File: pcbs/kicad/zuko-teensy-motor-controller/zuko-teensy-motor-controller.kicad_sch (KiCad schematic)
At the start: 58 parts, among them J1 Conn_01x03, J10 Conn_01x03, J11 Conn_01x03, J12 Conn_01x03, J13 Conn_01x03, J14 Conn_01x02, J15 Conn_01x02, J16 Conn_01x02, J17 Conn_01x03, J18 Conn_01x03, J19 Conn_01x02, J2 Conn_01x03, J20 Conn_01x02, J21 Conn_01x02, J22 Conn_01x03, J24 Conn_01x04, J25 Conn_01x03, J26 Conn_01x03, J27 Conn_01x04, J28 Conn_01x04, J29 Conn_01x04, J3 Conn_01x03, J30 Conn_01x04, J31 Conn_01x04, J32 Conn_01x04, J33 Conn_01x04, J4 Conn_01x02, J5 Conn_01x03, J6 Conn_01x03, J7 Conn_01x03, J8 Conn_01x03, J9 Conn_01x03, Q1 BSS138, Q2 BSS138, U1 ACS712xLCTR-20A, U2 Teensy4.0, U3 ULN2003

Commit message: pcb update
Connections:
- net AUX_M1: now also J17.1 (Pin_1); no longer J17.2 (Pin_2)
- net AUX_M2: now also J18.1 (Pin_1); no longer J18.2 (Pin_2)
- net AUX_M3: now also J22.1 (Pin_1); no longer J22.2 (Pin_2)
- new net: J17.2 (Pin_2), J18.2 (Pin_2), J22.2 (Pin_2), JP1.2 (C)

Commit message: pcb update
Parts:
- added J23: Conn_01x02, Connector_PinHeader_2.54mm:PinHeader_1x02_P2.54mm_Vertical, symbol Connector_Generic:Conn_01x02
- J4: footprint Connector_AMASS:AMASS_XT60-F_1x02_P7.20mm_Vertical -> Connector_AMASS:AMASS_XT60-M_1x02_P7.20mm_Vertical
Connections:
- net +BATT: now also J23.1 (Pin_1)
- net GND: now also J23.2 (Pin_2)
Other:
- moved on the sheet: J21

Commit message: pcb update
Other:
- note added: "Aux. Servo Motor Interfaces"
- note added: "Contact Switches and LEDs"
- note added: "I2C Interfaces"
- note added: "Microcontroller"
- note added: "Neopixel LED Strip Interfaces"
- note added: "Power In, Current Sense, and Voltage Sense"
- note added: "Servo Motor Interfaces"
- note added: "UART Interface"
- moved on the sheet: C1, C2, C3, C4, C5, C6, J1, J10, J11, J12, J13, J14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

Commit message: pcb update
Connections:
- net GND: no longer U2.47 (GND)
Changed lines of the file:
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@@
   (junction (at 105.41 181.61) (diameter 0) (color 0 0 0 0)
   )
-  (junction (at 265.43 149.86) (diameter 0) (color 0 0 0 0)
-  )
   (junction (at 83.82 114.3) (diameter 0) (color 0 0 0 0)
   )
@@
     (stroke (width 0) (type default) (color 0 0 0 0))
   )
-  (wire (pts (xy 265.43 106.68) (xy 265.43 149.86))
-    (stroke (width 0) (type default) (color 0 0 0 0))
-  )
   (wire (pts (xy 363.22 222.25) (xy 363.22 223.52))
     (stroke (width 0) (type default) (color 0 0 0 0))
@@
     (stroke (width 0) (type default) (color 0 0 0 0))
   )
-  (wire (pts (xy 247.65 106.68) (xy 265.43 106.68))
-    (stroke (width 0) (type default) (color 0 0 0 0))
-  )

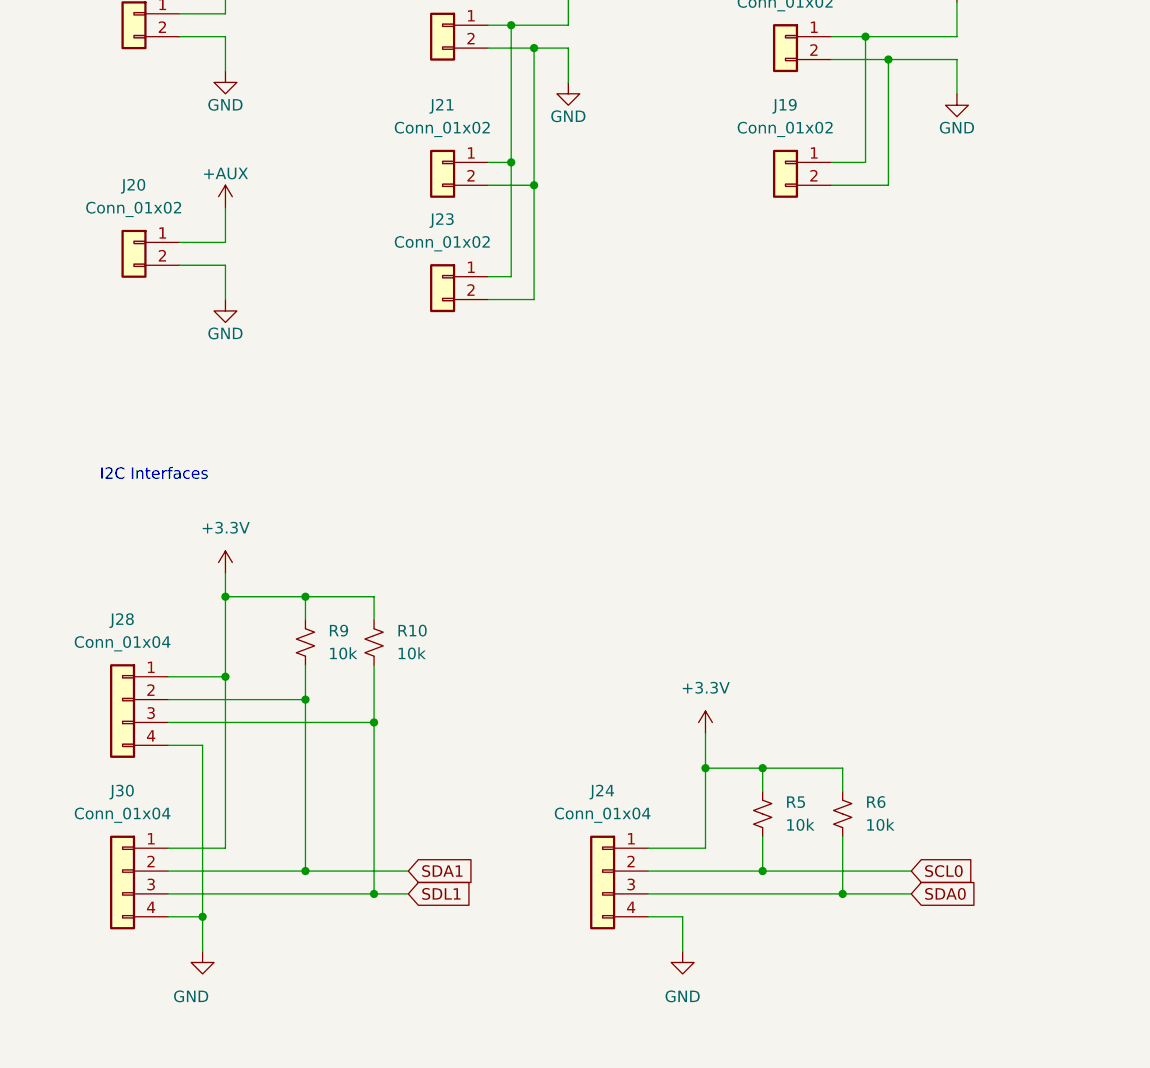
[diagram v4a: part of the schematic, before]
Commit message: pcb update - 2 layers to 4 layers
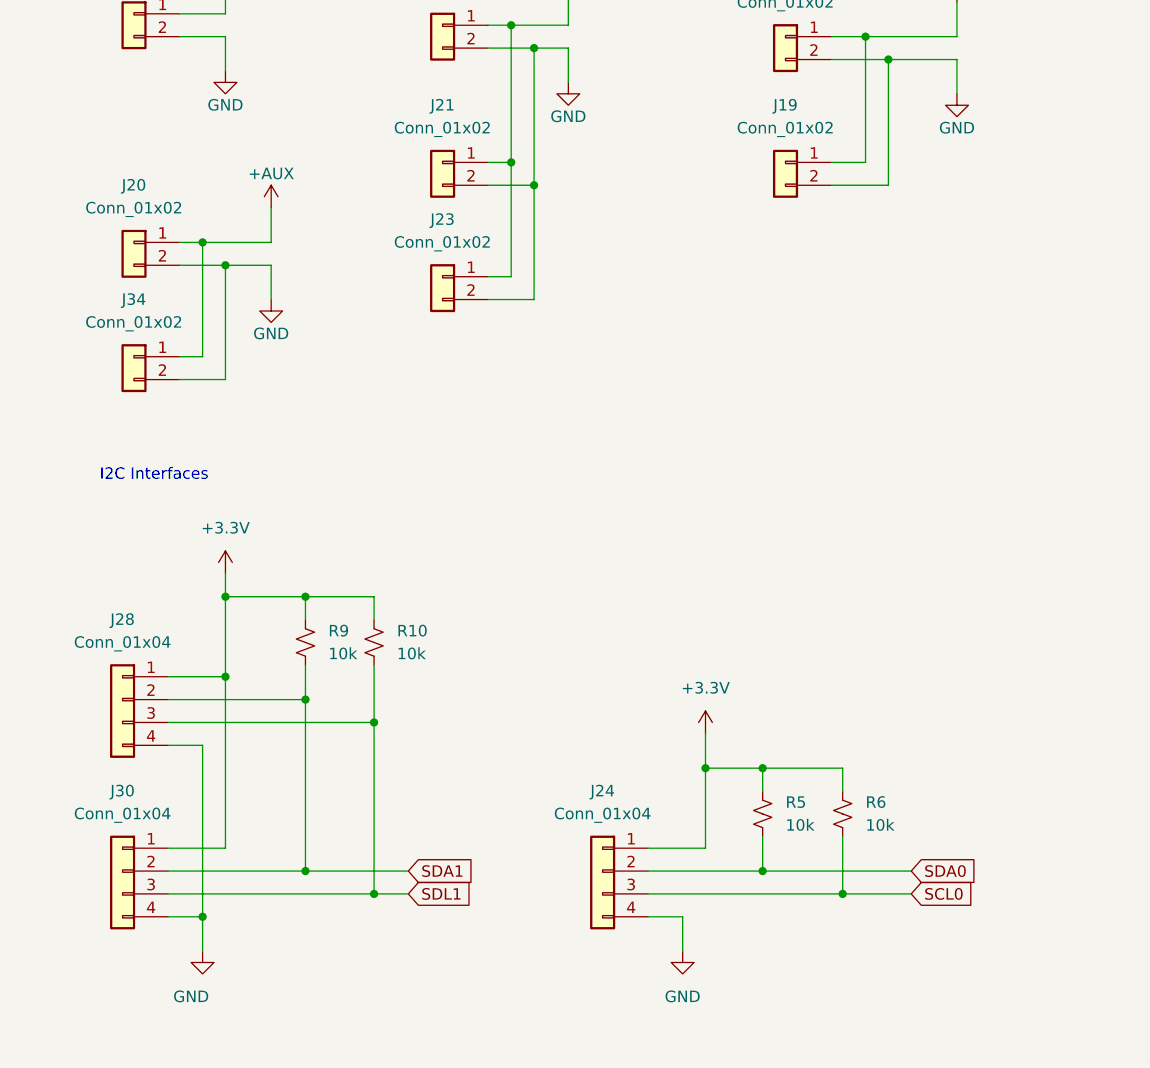
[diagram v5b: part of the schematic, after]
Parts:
- added J34: Conn_01x02, Connector_PinHeader_2.54mm:PinHeader_1x02_P2.54mm_Vertical, symbol Connector_Generic:Conn_01x02
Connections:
- net +AUX: now also J34.1 (Pin_1)
- net GND: now also J34.2 (Pin_2)
- net SCL0: now also J24.3 (Pin_3), R6.2; no longer J24.2 (Pin_2), R5.2
- net SDA0: now also J24.2 (Pin_2), R5.2; no longer J24.3 (Pin_3), R6.2
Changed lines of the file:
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@@
   (junction (at 241.3 210.82) (diameter 0) (color 0 0 0 0)
   )
-  (junction (at 120.65 195.58) (diameter 0) (color 0 0 0 0)
-  )
   (junction (at 86.36 116.84) (diameter 0) (color 0 0 0 0)
   )
@@
   (junction (at 237.49 57.15) (diameter 0) (color 0 0 0 0)
   )
-  (junction (at 111.76 193.04) (diameter 0) (color 0 0 0 0)
-  )
   (junction (at 109.22 46.99) (diameter 0) (color 0 0 0 0)
   )
   (junction (at 238.76 256.54) (diameter 0) (color 0 0 0 0)
   )
+  (junction (at 49.53 123.19) (diameter 0) (color 0 0 0 0)
+  )
   (junction (at 76.2 271.78) (diameter 0) (color 0 0 0 0)
   )
@@
   (junction (at 125.73 102.87) (diameter 0) (color 0 0 0 0)
   )
+  (junction (at 111.76 193.04) (diameter 0) (color 0 0 0 0)
+  )
   (junction (at 207.01 39.37) (diameter 0) (color 0 0 0 0)
   )
@@
   (junction (at 64.77 237.49) (diameter 0) (color 0 0 0 0)
   )
+  (junction (at 52.07 125.73) (diameter 0) (color 0 0 0 0)
+  )
+  (junction (at 120.65 195.58) (diameter 0) (color 0 0 0 0)
+  )
   (junction (at 68.58 31.75) (diameter 0) (color 0 0 0 0)
   )
@@
     (stroke (width 0) (type default) (color 0 0 0 0))
   )
+  (wire (pts (xy 46.99 135.89) (xy 49.53 135.89))
+    (stroke (width 0) (type default) (color 0 0 0 0))
+  )
   (wire (pts (xy 224.79 226.06) (xy 224.79 229.87))
     (stroke (width 0) (type default) (color 0 0 0 0))
@@
     (stroke (width 0) (type default) (color 0 0 0 0))
   )
-  (wire (pts (xy 111.76 193.04) (xy 128.27 193.04))
-    (stroke (width 0) (type default) (color 0 0 0 0))
-  )
   (wire (pts (xy 309.88 165.1) (xy 340.36 165.1))
     (stroke (width 0) (type default) (color 0 0 0 0))
@@
     (stroke (width 0) (type default) (color 0 0 0 0))
   )
+  (wire (pts (xy 52.07 125.73) (xy 57.15 125.73))
+    (stroke (width 0) (type default) (color 0 0 0 0))
+  )
   (wire (pts (xy 81.28 114.3) (xy 83.82 114.3))
     (stroke (width 0) (type default) (color 0 0 0 0))
@@
     (stroke (width 0) (type default) (color 0 0 0 0))
   )
+  (wire (pts (xy 120.65 195.58) (xy 128.27 195.58))
+    (stroke (width 0) (type default) (color 0 0 0 0))
+  )
   (wire (pts (xy 133.35 102.87) (xy 133.35 106.68))
     (stroke (width 0) (type default) (color 0 0 0 0))
@@
     (stroke (width 0) (type default) (color 0 0 0 0))
   )
+  (wire (pts (xy 52.07 138.43) (xy 52.07 125.73))
+    (stroke (width 0) (type default) (color 0 0 0 0))
+  )
   (wire (pts (xy 342.9 109.22) (xy 342.9 114.3))
     (stroke (width 0) (type default) (color 0 0 0 0))
@@
     (stroke (width 0) (type default) (color 0 0 0 0))
   )
+  (wire (pts (xy 46.99 138.43) (xy 52.07 138.43))
+    (stroke (width 0) (type default) (color 0 0 0 0))
+  )
   (wire (pts (xy 187.96 96.52) (xy 191.77 96.52))
     (stroke (width 0) (type default) (color 0 0 0 0))
@@
     (stroke (width 0) (type default) (color 0 0 0 0))
   )
-  (wire (pts (xy 52.07 123.19) (xy 52.07 119.38))
+  (wire (pts (xy 57.15 123.19) (xy 57.15 119.38))
     (stroke (width 0) (type default) (color 0 0 0 0))
   )
@@
     (stroke (width 0) (type default) (color 0 0 0 0))
   )
-  (wire (pts (xy 46.99 123.19) (xy 52.07 123.19))
+  (wire (pts (xy 46.99 123.19) (xy 49.53 123.19))
     (stroke (width 0) (type default) (color 0 0 0 0))
   )
@@
     (stroke (width 0) (type default) (color 0 0 0 0))
   )
+  (wire (pts (xy 111.76 193.04) (xy 128.27 193.04))
+    (stroke (width 0) (type default) (color 0 0 0 0))
+  )
   (wire (pts (xy 68.58 176.53) (xy 68.58 195.58))
     (stroke (width 0) (type default) (color 0 0 0 0))
@@
     (stroke (width 0) (type default) (color 0 0 0 0))
   )
+  (wire (pts (xy 49.53 135.89) (xy 49.53 123.19))
+    (stroke (width 0) (type default) (color 0 0 0 0))
+  )
   (wire (pts (xy 238.76 243.84) (xy 243.84 243.84))
     (stroke (width 0) (type default) (color 0 0 0 0))
@@
     (stroke (width 0) (type default) (color 0 0 0 0))
   )
+  (wire (pts (xy 49.53 123.19) (xy 57.15 123.19))
+    (stroke (width 0) (type default) (color 0 0 0 0))
+  )
   (wire (pts (xy 120.65 189.23) (xy 120.65 195.58))
     (stroke (width 0) (type default) (color 0 0 0 0))
@@
     (stroke (width 0) (type default) (color 0 0 0 0))
   )
-  (wire (pts (xy 120.65 195.58) (xy 128.27 195.58))
-    (stroke (width 0) (type default) (color 0 0 0 0))
-  )
   (wire (pts (xy 49.53 198.12) (xy 49.53 201.93))
     (stroke (width 0) (type default) (color 0 0 0 0))
@@
     (stroke (width 0) (type default) (color 0 0 0 0))
   )
-  (wire (pts (xy 52.07 125.73) (xy 52.07 129.54))
+  (wire (pts (xy 57.15 125.73) (xy 57.15 129.54))
     (stroke (width 0) (type default) (color 0 0 0 0))
   )
@@
     )
   )
-  (global_label "SCL0" (shape input) (at 128.27 193.04 0) (fields_autoplaced)
+  (global_label "SCL0" (shape input) (at 128.27 195.58 0) (fields_autoplaced)
     (effects (font (size 1.27 1.27)) (justify left))
-    (property "Intersheet References" "${INTERSHEET_REFS}" (id 0) (at 135.4002 192.9606 0)
+    (property "Intersheet References" "${INTERSHEET_REFS}" (id 0) (at 135.4002 195.6594 0)
       (effects (font (size 1.27 1.27)) (justify left) hide)
     )
@@
     )
   )
-  (global_label "SDA0" (shape input) (at 128.27 195.58 0) (fields_autoplaced)
+  (global_label "SDA0" (shape input) (at 128.27 193.04 0) (fields_autoplaced)
     (effects (font (size 1.27 1.27)) (justify left))
-    (property "Intersheet References" "${INTERSHEET_REFS}" (id 0) (at 135.4607 195.5006 0)
+    (property "Intersheet References" "${INTERSHEET_REFS}" (id 0) (at 135.4607 193.1194 0)
       (effects (font (size 1.27 1.27)) (justify left) hide)
     )
@@
     (pin "1")
   )
-  (symbol (lib_id "power:GND") (at 52.07 129.54 0) (unit 1)
+  (symbol (lib_id "power:GND") (at 57.15 129.54 0) (unit 1)
     (in_bom yes) (on_board yes)
-    (property "Reference" "#PWR048" (id 0) (at 52.07 135.89 0)
+    (property "Reference" "#PWR048" (id 0) (at 57.15 135.89 0)
       (effects (font (size 1.27 1.27)) hide)
     )
-    (property "Value" "GND" (id 1) (at 52.07 133.35 0))
-    (property "Footprint" "" (id 2) (at 52.07 129.54 0)
+    (property "Value" "GND" (id 1) (at 57.15 133.35 0))
+    (property "Footprint" "" (id 2) (at 57.15 129.54 0)
       (effects (font (size 1.27 1.27)) hide)
     )
-    (property "Datasheet" "" (id 3) (at 52.07 129.54 0)
+    (property "Datasheet" "" (id 3) (at 57.15 129.54 0)
       (effects (font (size 1.27 1.27)) hide)
     )
@@
     (pin "1")
   )
-  (symbol (lib_id "general:+AUX") (at 52.07 119.38 0) (unit 1)
+  (symbol (lib_id "general:+AUX") (at 57.15 119.38 0) (unit 1)
     (in_bom yes) (on_board yes)
-    (property "Reference" "#PWR046" (id 0) (at 52.07 123.19 0)
+    (property "Reference" "#PWR046" (id 0) (at 57.15 123.19 0)
       (effects (font (size 1.27 1.27)) hide)
     )
-    (property "Value" "+AUX" (id 1) (at 52.07 115.57 0))
-    (property "Footprint" "" (id 2) (at 52.07 119.38 0)
+    (property "Value" "+AUX" (id 1) (at 57.15 115.57 0))
+    (property "Footprint" "" (id 2) (at 57.15 119.38 0)
       (effects (font (size 1.27 1.27)) hide)
     )
-    (property "Datasheet" "" (id 3) (at 52.07 119.38 0)
+    (property "Datasheet" "" (id 3) (at 57.15 119.38 0)
       (effects (font (size 1.27 1.27)) hide)
     )
@@
     (pin "1")
   )
+  (symbol (lib_id "Connector_Generic:Conn_01x02") (at 41.91 135.89 0) (mirror y) (unit 1)
+    (in_bom yes) (on_board yes) (fields_autoplaced)
+    (property "Reference" "J34" (id 0) (at 41.91 129.54 0))
+    (property "Value" "Conn_01x02" (id 1) (at 41.91 132.08 0))
+    (property "Footprint" "Connector_PinHeader_2.54mm:PinHeader_1x02_P2.54mm_Vertical" (id 2) (at 41.91 135.89 0)
+      (effects (font (size 1.27 1.27)) hide)
+    )
+    (property "Datasheet" "~" (id 3) (at 41.91 135.89 0)
+      (effects (font (size 1.27 1.27)) hide)
+    )
+    (pin "1")
+    (pin "2")
+  )
   (sheet_instances
     (path "/" (page "1"))
@@
       (reference "J33") (unit 1) (value "Conn_01x04") (footprint "Connector_PinHeader_2.54mm:PinHeader_1x04_P2.54mm_Vertical")
     )
+    (path "/ff97544e-df17-42d7-9448-14711d2341b5"
+      (reference "J34") (unit 1) (value "Conn_01x02") (footprint "Connector_PinHeader_2.54mm:PinHeader_1x02_P2.54mm_Vertical")
+    )
     (path "/524d0364-d302-44d0-a8e7-0c61adea6480"

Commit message: pcb update
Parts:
- added JP2, JP3: Jumper_3_Open, Connector_PinHeader_2.54mm:PinHeader_1x03_P2.54mm_Vertical, symbol Jumper:Jumper_3_Open
- R3: value 10k -> 20k
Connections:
- net +AUX: now also JP2.3 (B), JP3.3 (B)
- net +BATT: now also JP2.1 (A), JP3.1 (A)
- net at J18.2 (Pin_2), JP1.2 (C): no longer J17.2 (Pin_2), J22.2 (Pin_2)
- new net: J17.2 (Pin_2), JP2.2 (C)
- new net: J22.2 (Pin_2), JP3.2 (C)
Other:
- note added: "Battery Connector"
- note added: "Extra Power Connections"
- note removed: "Misc. Peripheral Power"
- moved on the sheet: J15, J16, J19, J21, J23, J24, J28, J30, J34, JP1, R10, R5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

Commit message: update notes
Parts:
- J4: footprint Connector_AMASS:AMASS_XT60-M_1x02_P7.20mm_Vertical -> Connector_AMASS:AMASS_XT30U-M_1x02_P5.0mm_Vertical
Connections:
- net GND: now also J4.1 (Pin_1); no longer J4.2 (Pin_2)
- net at U1.1 (IP+), U1.2 (IP+): now also J4.2 (Pin_2); no longer J4.1 (Pin_1)
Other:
- moved on the sheet: J4
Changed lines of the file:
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@@
     (stroke (width 0) (type default) (color 0 0 0 0))
   )
+  (wire (pts (xy 40.64 41.91) (xy 58.42 41.91))
+    (stroke (width 0) (type default) (color 0 0 0 0))
+  )
   (wire (pts (xy 379.73 171.45) (xy 382.27 171.45))
     (stroke (width 0) (type default) (color 0 0 0 0))
@@
     (stroke (width 0) (type default) (color 0 0 0 0))
   )
-  (wire (pts (xy 40.64 41.91) (xy 58.42 41.91))
-    (stroke (width 0) (type default) (color 0 0 0 0))
-  )
   (wire (pts (xy 50.8 255.27) (xy 46.99 255.27))
     (stroke (width 0) (type default) (color 0 0 0 0))
@@
     (stroke (width 0) (type default) (color 0 0 0 0))
   )
-  (wire (pts (xy 40.64 44.45) (xy 43.18 44.45))
-    (stroke (width 0) (type default) (color 0 0 0 0))
-  )
   (wire (pts (xy 342.9 69.85) (xy 345.44 69.85))
     (stroke (width 0) (type default) (color 0 0 0 0))
@@
     (stroke (width 0) (type default) (color 0 0 0 0))
   )
+  (wire (pts (xy 43.18 39.37) (xy 40.64 39.37))
+    (stroke (width 0) (type default) (color 0 0 0 0))
+  )
   (wire (pts (xy 76.2 241.3) (xy 76.2 234.95))
     (stroke (width 0) (type default) (color 0 0 0 0))
@@
     (stroke (width 0) (type default) (color 0 0 0 0))
   )
-  (wire (pts (xy 43.18 44.45) (xy 43.18 63.5))
+  (wire (pts (xy 43.18 39.37) (xy 43.18 63.5))
     (stroke (width 0) (type default) (color 0 0 0 0))
   )
@@
     (effects (font (size 1.27 1.27)) (justify left bottom))
   )
-  (text "Battery Connector" (at 29.21 33.02 0)
+  (text "Battery Connector" (at 29.21 30.48 0)
     (effects (font (size 1.27 1.27)) (justify left bottom))
   )
@@
     (pin "1")
   )
-  (symbol (lib_id "Connector_Generic:Conn_01x02") (at 35.56 41.91 0) (mirror y) (unit 1)
-    (in_bom yes) (on_board yes) (fields_autoplaced)
-    (property "Reference" "J4" (id 0) (at 35.56 35.56 0))
-    (property "Value" "Conn_01x02" (id 1) (at 35.56 38.1 0))
-    (property "Footprint" "Connector_AMASS:AMASS_XT60-M_1x02_P7.20mm_Vertical" (id 2) (at 35.56 41.91 0)
-      (effects (font (size 1.27 1.27)) hide)
-    )
-    (property "Datasheet" "~" (id 3) (at 35.56 41.91 0)
+  (symbol (lib_id "Connector_Generic:Conn_01x02") (at 35.56 39.37 0) (mirror y) (unit 1)
+    (in_bom yes) (on_board yes)
+    (property "Reference" "J4" (id 0) (at 35.56 33.02 0))
+    (property "Value" "Conn_01x02" (id 1) (at 35.56 35.56 0))
+    (property "Footprint" "Connector_AMASS:AMASS_XT30U-M_1x02_P5.0mm_Vertical" (id 2) (at 35.56 45.72 0))
+    (property "Datasheet" "~" (id 3) (at 35.56 39.37 0)
       (effects (font (size 1.27 1.27)) hide)
     )
@@
     )
     (path "/61310d07-f50a-454d-9e28-083c9236557f"
-      (reference "J4") (unit 1) (value "Conn_01x02") (footprint "Connector_AMASS:AMASS_XT60-M_1x02_P7.20mm_Vertical")
+      (reference "J4") (unit 1) (value "Conn_01x02") (footprint "Connector_AMASS:AMASS_XT30U-M_1x02_P5.0mm_Vertical")
     )
     (path "/f3580d19-90a5-4be5-9be0-4ac824637a50"
